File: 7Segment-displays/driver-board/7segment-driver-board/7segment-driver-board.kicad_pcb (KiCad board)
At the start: 2 copper layers, 40 x 16 mm, 10 parts, among them IC1 MAX7219CWG, P1 Ext PWR, P2 DataIn, P3 DataOut, P4 D0-D5

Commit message: update marking on back side
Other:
- board text added: "www.MobiFlight.com V1.0"
- board text removed: "MobiFlight V1.0"
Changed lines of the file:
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@@
 		)
 	)
-	(gr_text "MobiFlight\nV1.0"
-		(at 108.593764 117.4 0)
+	(gr_text "www.MobiFlight.com\nV1.0"
+		(at 108.593763 117.398774 0)
 		(layer "B.SilkS")
 		(effects

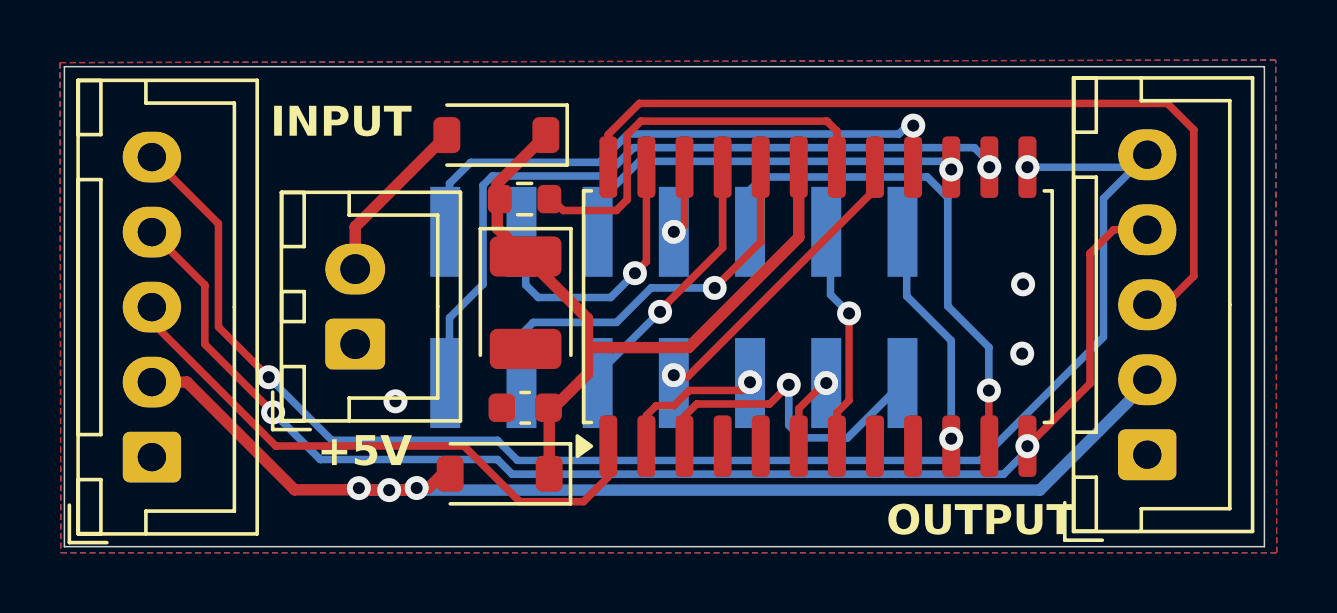
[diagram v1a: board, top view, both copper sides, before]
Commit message: better routing for handsoldering connector on backside
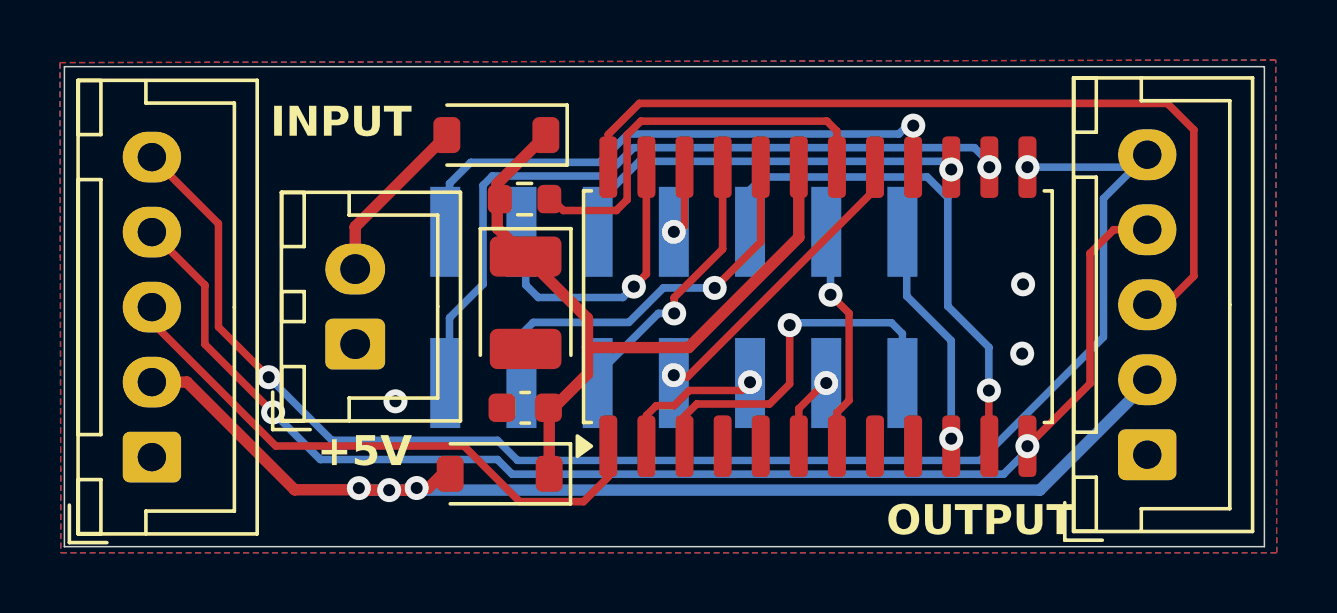
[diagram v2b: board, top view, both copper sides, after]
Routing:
- net /DIG_4: track 11.0 -> 12.5 mm
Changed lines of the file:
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@@
+	)
+	(segment
+		(start 109.264496 113.175504)
+		(end 109.264496 114.175905)
+		(width 0.25)
+		(layer "F.Cu")
+		(net 10)
+	)
+	(segment
+		(start 112.77 110.14)
+		(end 112.77 112.1)
+		(width 0.25)
+		(layer "F.Cu")
+		(net 10)
+	)
+	(segment
+		(start 112.77 112.1)
+		(end 112.1 112.77)
+		(width 0.25)
+		(layer "F.Cu")
+		(net 10)
+	)
+	(segment
+		(start 112.1 112.77)
+		(end 111.14775 112.77)
+		(width 0.25)
+		(layer "F.Cu")
+		(net 10)
+	)
+	(segment
+		(start 111.14775 112.77)
+		(end 111.14675 112.769)
+		(width 0.25)
+		(layer "F.Cu")
+		(net 10)
+	)
+	(segment
+		(start 109.671 112.769)
+		(end 109.264496 113.175504)
+		(width 0.25)
+		(layer "F.Cu")
+		(net 10)
 	)
 	(segment
 		(start 111.14675 112.769)
-		(end 111.14775 112.77)
-		(width 0.25)
-		(layer "F.Cu")
-		(net 10)
-	)
-	(segment
-		(start 109.264496 114.175905)
-		(end 109.264496 113.175504)
-		(width 0.25)
-		(layer "F.Cu")
-		(net 10)
-	)
-	(segment
-		(start 109.264496 113.175504)
 		(end 109.671 112.769)
-		(width 0.25)
-		(layer "F.Cu")
-		(net 10)
-	)
-	(segment
-		(start 112.1 112.77)
-		(end 112.74 112.13)
-		(width 0.25)
-		(layer "F.Cu")
-		(net 10)
-	)
-	(segment
-		(start 109.671 112.769)
-		(end 111.14675 112.769)
-		(width 0.25)
-		(layer "F.Cu")
-		(net 10)
-	)
-	(segment
-		(start 111.14775 112.77)
-		(end 112.1 112.77)
 		(width 0.25)
 		(layer "F.Cu")
@@
 	)
 	(via
-		(at 112.74 112.13)
+		(at 112.77 110.14)
 		(size 0.8)
 		(drill 0.4)
@@
 	(segment
 		(start 116.52847 112.071106)
-		(end 114.70047 113.899106)
-		(width 0.254)
-		(layer "B.Cu")
-		(net 10)
-	)
-	(segment
-		(start 114.70047 113.899106)
-		(end 113.16047 113.899106)
-		(width 0.254)
-		(layer "B.Cu")
-		(net 10)
-	)
-	(segment
-		(start 113.16047 113.899106)
-		(end 112.74 113.478636)
-		(width 0.254)
-		(layer "B.Cu")
-		(net 10)
-	)
-	(segment
-		(start 112.74 113.478636)
-		(end 112.74 112.13)
-		(width 0.254)
+		(end 116.52847 110.42847)
+		(width 0.25)
+		(layer "B.Cu")
+		(net 10)
+	)
+	(segment
+		(start 112.85 110.06)
+		(end 112.77 110.14)
+		(width 0.25)
+		(layer "B.Cu")
+		(net 10)
+	)
+	(segment
+		(start 116.52847 110.42847)
+		(end 116.16 110.06)
+		(width 0.25)
+		(layer "B.Cu")
+		(net 10)
+	)
+	(segment
+		(start 116.16 110.06)
+		(end 112.85 110.06)
+		(width 0.25)
 		(layer "B.Cu")
 		(net 10)
@@
 	)
 	(segment
-		(start 107.611999 108.408001)
-		(end 107.994496 108.025504)
-		(width 0.254)
-		(layer "F.Cu")
-		(net 13)
-	)
-	(segment
-		(start 107.611999 108.409867)
-		(end 107.611999 108.408001)
-		(width 0.254)
-		(layer "F.Cu")
-		(net 13)
-	)
-	(segment
-		(start 107.994496 108.025504)
+		(start 107.994496 108.43737)
 		(end 107.994496 104.875905)
 		(width 0.254)
@@
 		(net 13)
 	)
-	(via
-		(at 107.611999 108.409867)
-		(size 0.8)
-		(drill 0.4)
-		(layers "F.Cu" "B.Cu")
-		(net 13)
-	)
-	(segment
-		(start 107.611999 108.409867)
-		(end 106.801866 109.22)
+	(segment
+		(start 107.575933 108.855933)
+		(end 107.994496 108.43737)
+		(width 0.254)
+		(layer "F.Cu")
+		(net 13)
+	)
+	(via
+		(at 107.575933 108.855933)
+		(size 0.8)
+		(drill 0.4)
+		(layers "F.Cu" "B.Cu")
+		(net 13)
+	)
+	(segment
+		(start 107.575933 108.855933)
+		(end 107.211866 109.22)
+		(width 0.254)
+		(layer "B.Cu")
+		(net 13)
+	)
+	(segment
+		(start 103.972 107.174636)
+		(end 103.82847 107.031106)
+		(width 0.254)
+		(layer "B.Cu")
+		(net 13)
+	)
+	(segment
+		(start 103.972 108.802)
+		(end 103.972 107.174636)
 		(width 0.254)
 		(layer "B.Cu")
@@
 	)
 	(segment
-		(start 104.39 109.22)
-		(end 106.801866 109.22)
-		(width 0.254)
-		(layer "B.Cu")
-		(net 13)
-	)
-	(segment
-		(start 103.972 108.802)
-		(end 103.972 107.174636)
-		(width 0.254)
-		(layer "B.Cu")
-		(net 13)
-	)
-	(segment
-		(start 103.972 107.174636)
-		(end 103.82847 107.031106)
+		(start 107.211866 109.22)
+		(end 104.39 109.22)
 		(width 0.254)
 		(layer "B.Cu")
@@
 	)
 	(segment
-		(start 114.75 109.75)
+		(start 114.75 112.65)
+		(end 114.344496 113.055504)
+		(width 0.25)
+		(layer "F.Cu")
+		(net 15)
+	)
+	(segment
+		(start 114.132 109.128)
+		(end 114.75 109.746)
+		(width 0.25)
+		(layer "F.Cu")
+		(net 15)
+	)
+	(segment
+		(start 114.75 109.746)
 		(end 114.75 112.65)
 		(width 0.25)
@@
 		(net 15)
 	)
-	(segment
-		(start 114.75 112.65)
-		(end 114.344496 113.055504)
-		(width 0.25)
-		(layer "F.Cu")
-		(net 15)
-	)
-	(via
-		(at 114.75 109.75)
+	(via
+		(at 114.132 109.128)
 		(size 0.8)
 		(drill 0.4)
@@
 	)
 	(segment
-		(start 114.75 109.746)
-		(end 114.132 109.128)
-		(width 0.254)
-		(layer "B.Cu")
-		(net 15)
-	)
-	(segment
 		(start 114.132 107.174636)
 		(end 113.98847 107.031106)
@@
 	)
 	(segment
-		(start 114.75 109.75)
-		(end 114.75 109.746)
-		(width 0.254)
-		(layer "B.Cu")
-		(net 15)
-	)
-	(segment
 		(start 109.264496 106.830775)
 		(end 109.264496 104.875905)
@@
 	)
 	(segment
+		(start 108.56 108.9)
+		(end 107.41 110.05)
+		(width 0.254)
+		(layer "B.Cu")
+		(net 17)
+	)
+	(segment
+		(start 104.22 110.05)
+		(end 103.82847 110.44153)
+		(width 0.254)
+		(layer "B.Cu")
+		(net 17)
+	)
+	(segment
+		(start 110.27 108.9)
+		(end 108.56 108.9)
+		(width 0.254)
+		(layer "B.Cu")
+		(net 17)
+	)
+	(segment
 		(start 103.82847 111.939741)
 		(end 103.972 112.083271)
@@
 	)
 	(segment
-		(start 110.27 108.9)
-		(end 108.15 108.9)
+		(start 107.41 110.05)
+		(end 104.22 110.05)
 		(width 0.254)
 		(layer "B.Cu")
@@
 	)
 	(segment
-		(start 107 110.05)
-		(end 104.22 110.05)
-		(width 0.254)
-		(layer "B.Cu")
-		(net 17)
-	)
-	(segment
-		(start 108.15 108.9)
-		(end 107 110.05)
-		(width 0.254)
-		(layer "B.Cu")
-		(net 17)
-	)
-	(segment
-		(start 104.22 110.05)
-		(end 103.82847 110.44153)
-		(width 0.254)
-		(layer "B.Cu")
-		(net 17)
-	)
-	(segment
-		(start 110.534496 107.565504)
+		(start 110.534496 107.605956)
 		(end 110.534496 104.875905)
 		(width 0.254)
@@
 	)
 	(segment
-		(start 108.69 109.458224)
-		(end 108.69 109.41)
-		(width 0.254)
-		(layer "F.Cu")
-		(net 19)
-	)
-	(segment
-		(start 108.69 109.41)
-		(end 110.534496 107.565504)
-		(width 0.254)
-		(layer "F.Cu")
-		(net 19)
-	)
-	(segment
-		(start 108.45 109.698224)
-		(end 108.69 109.458224)
-		(width 0.254)
-		(layer "F.Cu")
-		(net 19)
-	)
-	(via
-		(at 108.45 109.698224)
+		(start 108.92 109.75)
+		(end 108.92 109.220452)
+		(width 0.254)
+		(layer "F.Cu")
+		(net 19)
+	)
+	(segment
+		(start 108.92 109.220452)
+		(end 110.534496 107.605956)
+		(width 0.254)
+		(layer "F.Cu")
+		(net 19)
+	)
+	(via
+		(at 108.92 109.75)
 		(size 0.8)
 		(drill 0.4)
@@
 	)
 	(segment
+		(start 108.92 109.75)
+		(end 108.39 109.75)
+		(width 0.254)
+		(layer "B.Cu")
+		(net 19)
+	)
+	(segment
 		(start 106.380635 112.083271)
 		(end 106.512 112.083271)
@@
 	)
 	(segment
-		(start 108.441776 109.698224)
+		(start 108.39 109.75)
 		(end 106.36847 111.77153)
 		(width 0.254)
 		(layer "B.Cu")
-		(net 19)
-	)
-	(segment
-		(start 108.45 109.698224)
-		(end 108.441776 109.698224)
-		(width 0.254)
-		(layer "B.Cu")

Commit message: improved routing, fixed wrong marking
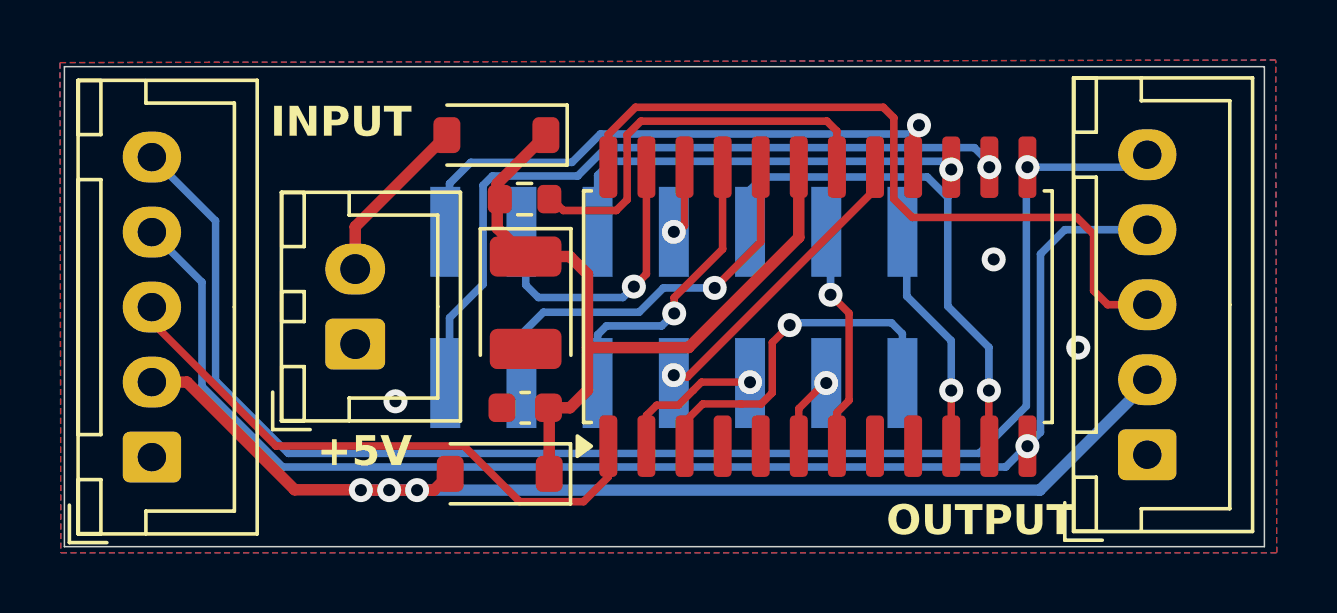
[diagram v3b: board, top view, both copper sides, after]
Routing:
- net /DOut: track 29.4 -> 26.1 mm
- net /Sel: track 44.7 -> 46.1 mm, vias 2 -> 1
- net /Clk: track 50.9 -> 49.6 mm, vias 2 -> 1
- net VCC: track 24.9 -> 26.1 mm
- net /SEG_E: track 9.38 -> 10.1 mm
- net /SEG_F: track 13.6 -> 14.2 mm
